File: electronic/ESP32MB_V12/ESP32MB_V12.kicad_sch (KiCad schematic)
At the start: 11 parts, among them J1 Conn_01x03_Socket, J2 Conn_01x04_Pin, J3 VESC_PWM, J4 BTN_UP, J5 BTN_DOWN, J6 Conn_01x05_Pin, J7 Conn_01x03_Pin, J8 Conn_01x04_Pin, J9 Conn_01x03_Pin, U1 MH-ET-ESP32-DEVKIT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

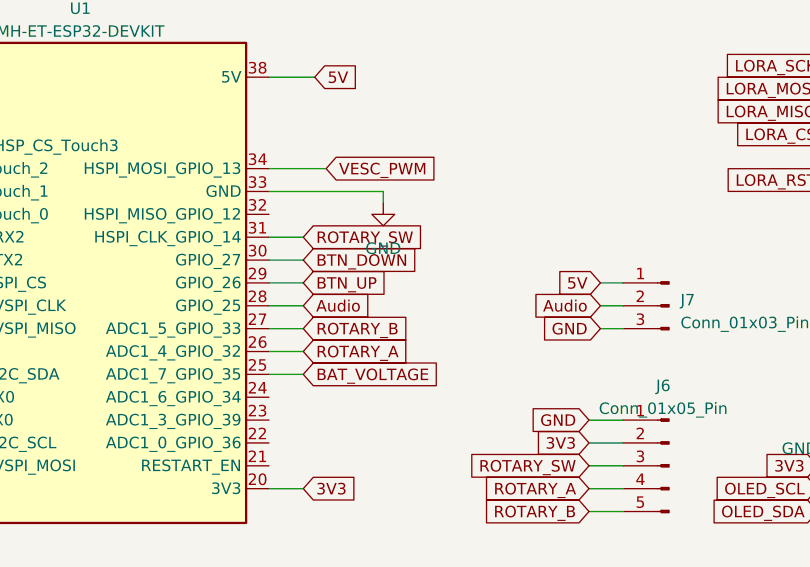
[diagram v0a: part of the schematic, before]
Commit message: added wind direction sensor to receiver
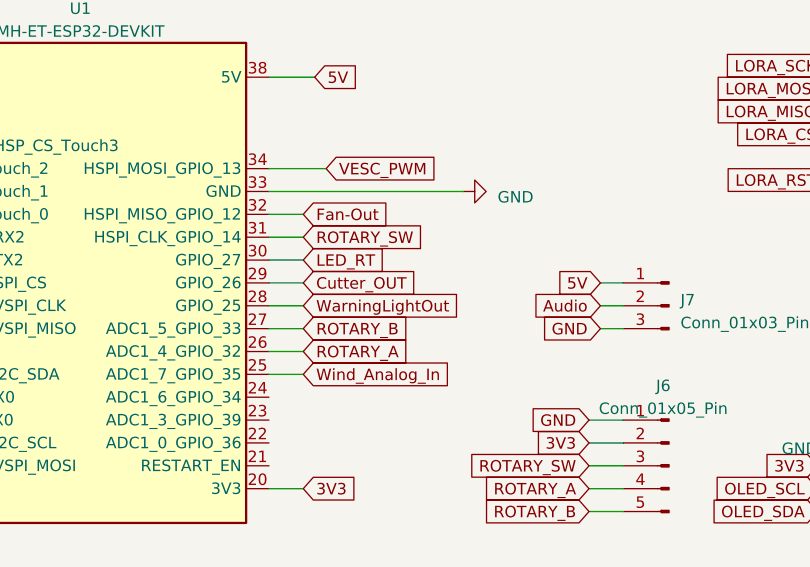
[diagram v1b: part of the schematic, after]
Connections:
- net Audio: no longer U1.28 (GPIO_25)
- net BTN_DOWN: no longer U1.30 (GPIO_27)
- net BTN_UP: no longer U1.29 (GPIO_26)
- net Fan-Out: now reaches U1.32 (HSPI_MISO_GPIO_12)
- net BAT_VOLTAGE renamed Wind_Analog_In
- new net Cutter_OUT: U1.29 (GPIO_26)
- new net LED_RT: U1.30 (GPIO_27)
- new net WarningLightOut: U1.28 (GPIO_25)
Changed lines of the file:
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@@
+    (stroke (width 0) (type default))
+  )
+  (wire (pts (xy 85.09 62.23) (xy 88.9 62.23))
     (stroke (width 0) (type default))
   )
@@
     (stroke (width 0) (type default))
   )
-  (wire (pts (xy 97.79 59.69) (xy 85.09 59.69))
+  (wire (pts (xy 106.68 59.69) (xy 85.09 59.69))
     (stroke (width 0) (type default))
   )
@@
     (stroke (width 0) (type default))
   )
-  (wire (pts (xy 97.79 59.69) (xy 97.79 60.96))
-    (stroke (width 0) (type default))
-  )
   (wire (pts (xy 39.37 118.11) (xy 45.72 118.11))
     (stroke (width 0) (type default))
@@
     )
   )
-  (global_label "BTN_DOWN" (shape input) (at 88.9 67.31 0) (fields_autoplaced)
-    (effects (font (size 1.27 1.27)) (justify left))
-    (property "Intersheetrefs" "${INTERSHEET_REFS}" (at 101.7239 67.31 0)
+  (global_label "LED_RT" (shape input) (at 88.9 67.31 0) (fields_autoplaced)
+    (effects (font (size 1.27 1.27)) (justify left))
+    (property "Intersheetrefs" "${INTERSHEET_REFS}" (at 98.4581 67.31 0)
       (effects (font (size 1.27 1.27)) (justify left) hide)
     )
@@
     )
   )
-  (global_label "BAT_VOLTAGE" (shape input) (at 88.9 80.01 0) (fields_autoplaced)
-    (effects (font (size 1.27 1.27)) (justify left))
-    (property "Intersheetrefs" "${INTERSHEET_REFS}" (at 104.022 80.01 0)
+  (global_label "Wind_Analog_In" (shape input) (at 88.9 80.01 0) (fields_autoplaced)
+    (effects (font (size 1.27 1.27)) (justify left))
+    (property "Intersheetrefs" "${INTERSHEET_REFS}" (at 106.1988 80.01 0)
       (effects (font (size 1.27 1.27)) (justify left) hide)
     )
@@
     )
   )
+  (global_label "Fan-Out" (shape input) (at 88.9 62.23 0) (fields_autoplaced)
+    (effects (font (size 1.27 1.27)) (justify left))
+    (property "Intersheetrefs" "${INTERSHEET_REFS}" (at 99.97 62.23 0)
+      (effects (font (size 1.27 1.27)) (justify left) hide)
+    )
+  )
   (global_label "LORA_MOSI" (shape input) (at 35.56 90.17 180) (fields_autoplaced)
     (effects (font (size 1.27 1.27)) (justify right))
@@
     )
   )
-  (global_label "Audio" (shape input) (at 88.9 72.39 0) (fields_autoplaced)
-    (effects (font (size 1.27 1.27)) (justify left))
-    (property "Intersheetrefs" "${INTERSHEET_REFS}" (at 96.9462 72.39 0)
+  (global_label "WarningLightOut" (shape input) (at 88.9 72.39 0) (fields_autoplaced)
+    (effects (font (size 1.27 1.27)) (justify left))
+    (property "Intersheetrefs" "${INTERSHEET_REFS}" (at 107.106 72.39 0)
       (effects (font (size 1.27 1.27)) (justify left) hide)
     )
@@
     )
   )
-  (global_label "BTN_UP" (shape input) (at 88.9 69.85 0) (fields_autoplaced)
-    (effects (font (size 1.27 1.27)) (justify left))
-    (property "Intersheetrefs" "${INTERSHEET_REFS}" (at 98.942 69.85 0)
+  (global_label "Cutter_OUT" (shape input) (at 88.9 69.85 0) (fields_autoplaced)
+    (effects (font (size 1.27 1.27)) (justify left))
+    (property "Intersheetrefs" "${INTERSHEET_REFS}" (at 102.1472 69.85 0)
       (effects (font (size 1.27 1.27)) (justify left) hide)
     )
@@
     (pin "1")
     (instances
-      (project "ESP32_MB"
+      (project "ESP32MB_V12"
         (path "/bf7aea9f-c323-4181-9607-ea95f9bf6702"
           (reference "#PWR04") (unit 1)
@@
     (pin "1")
     (instances
-      (project "ESP32_MB"
+      (project "ESP32MB_V12"
         (path "/bf7aea9f-c323-4181-9607-ea95f9bf6702"
           (reference "#PWR06") (unit 1)
@@
     (pin "1")
     (instances
-      (project "ESP32_MB"
+      (project "ESP32MB_V12"
         (path "/bf7aea9f-c323-4181-9607-ea95f9bf6702"
           (reference "#PWR01") (unit 1)
@@
     (pin "9")
     (instances
-      (project "ESP32_MB"
+      (project "ESP32MB_V12"
         (path "/bf7aea9f-c323-4181-9607-ea95f9bf6702"
           (reference "U2") (unit 1)
@@
     (pin "4")
     (instances
-      (project "ESP32_MB"
+      (project "ESP32MB_V12"
         (path "/bf7aea9f-c323-4181-9607-ea95f9bf6702"
           (reference "J2") (unit 1)
@@
     (pin "1")
     (instances
-      (project "ESP32_MB"
+      (project "ESP32MB_V12"
         (path "/bf7aea9f-c323-4181-9607-ea95f9bf6702"
           (reference "#PWR07") (unit 1)
@@
     (pin "3")
     (instances
-      (project "ESP32_MB"
+      (project "ESP32MB_V12"
         (path "/bf7aea9f-c323-4181-9607-ea95f9bf6702"
           (reference "J7") (unit 1)
@@
     (pin "2")
     (instances
-      (project "ESP32_MB"
+      (project "ESP32MB_V12"
         (path "/bf7aea9f-c323-4181-9607-ea95f9bf6702"
           (reference "J3") (unit 1)
@@
     (pin "4")
     (instances
-      (project "ESP32_MB"
+      (project "ESP32MB_V12"
         (path "/bf7aea9f-c323-4181-9607-ea95f9bf6702"
           (reference "J8") (unit 1)
@@
     (pin "3")
     (instances
-      (project "ESP32_MB"
+      (project "ESP32MB_V12"
         (path "/bf7aea9f-c323-4181-9607-ea95f9bf6702"
           (reference "J9") (unit 1)
@@
     (pin "9")
     (instances
-      (project "ESP32_MB"
+      (project "ESP32MB_V12"
         (path "/bf7aea9f-c323-4181-9607-ea95f9bf6702"
           (reference "U1") (unit 1)
@@
     (pin "1")
     (instances
-      (project "ESP32_MB"
+      (project "ESP32MB_V12"
         (path "/bf7aea9f-c323-4181-9607-ea95f9bf6702"
           (reference "#PWR05") (unit 1)
@@
     (pin "3")
     (instances
-      (project "ESP32_MB"
+      (project "ESP32MB_V12"
         (path "/bf7aea9f-c323-4181-9607-ea95f9bf6702"
           (reference "J1") (unit 1)
@@
     (pin "2")
     (instances
-      (project "ESP32_MB"
+      (project "ESP32MB_V12"
         (path "/bf7aea9f-c323-4181-9607-ea95f9bf6702"
           (reference "J5") (unit 1)
@@
     (pin "5")
     (instances
-      (project "ESP32_MB"
+      (project "ESP32MB_V12"
         (path "/bf7aea9f-c323-4181-9607-ea95f9bf6702"
           (reference "J6") (unit 1)
@@
     (pin "1")
     (instances
-      (project "ESP32_MB"
+      (project "ESP32MB_V12"
         (path "/bf7aea9f-c323-4181-9607-ea95f9bf6702"
           (reference "#PWR02") (unit 1)
@@
     )
   )
-  (symbol (lib_id "power:GND") (at 97.79 60.96 0) (unit 1)
-    (in_bom yes) (on_board yes) (dnp no) (fields_autoplaced)
-    (property "Reference" "#PWR03" (at 97.79 67.31 0)
-      (effects (font (size 1.27 1.27)) hide)
-    )
-    (property "Value" "GND" (at 97.79 66.04 0)
-      (effects (font (size 1.27 1.27)))
-    )
-    (property "Footprint" "" (at 97.79 60.96 0)
-      (effects (font (size 1.27 1.27)) hide)
-    )
-    (property "Datasheet" "" (at 97.79 60.96 0)
-      (effects (font (size 1.27 1.27)) hide)
-    )
-    (pin "1")
-    (instances
-      (project "ESP32_MB"
+  (symbol (lib_id "power:GND") (at 106.68 59.69 90) (unit 1)
+    (in_bom yes) (on_board yes) (dnp no) (fields_autoplaced)
+    (property "Reference" "#PWR03" (at 113.03 59.69 0)
+      (effects (font (size 1.27 1.27)) hide)
+    )
+    (property "Value" "GND" (at 110.49 60.325 90)
+      (effects (font (size 1.27 1.27)) (justify right))
+    )
+    (property "Footprint" "" (at 106.68 59.69 0)
+      (effects (font (size 1.27 1.27)) hide)
+    )
+    (property "Datasheet" "" (at 106.68 59.69 0)
+      (effects (font (size 1.27 1.27)) hide)
+    )
+    (pin "1")
+    (instances
+      (project "ESP32MB_V12"
         (path "/bf7aea9f-c323-4181-9607-ea95f9bf6702"
           (reference "#PWR03") (unit 1)
@@
     (pin "2")
     (instances
-      (project "ESP32_MB"
+      (project "ESP32MB_V12"
         (path "/bf7aea9f-c323-4181-9607-ea95f9bf6702"
           (reference "J4") (unit 1)
